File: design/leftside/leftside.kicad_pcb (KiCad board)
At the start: 4 copper layers, 142.6 x 96.2 mm, 227 parts, among them IC2 XC9148G50CER-G, IC3 nRF52833-QDAA-R7, IC4 74AHCT125PW,118, IC5 MCP23018T-E_SS, IC6 XC9291B33D1R-G, J1 USB_C_Receptacle_USB2.0_16P, J2 Battery Pos, J3 Battery Neg, J4 OLED_128x32, J6 Conn_01x04, J7 F32Q-1A7H1-11012, U1 BQ27441-G1, U2 BQ24072RGT, U3 USB6B1, U5 PEC11L-4015F-S0015, U6 PEC11L-4015F-S0015, Y1 ECS-320-8-37B2-JTY-TR

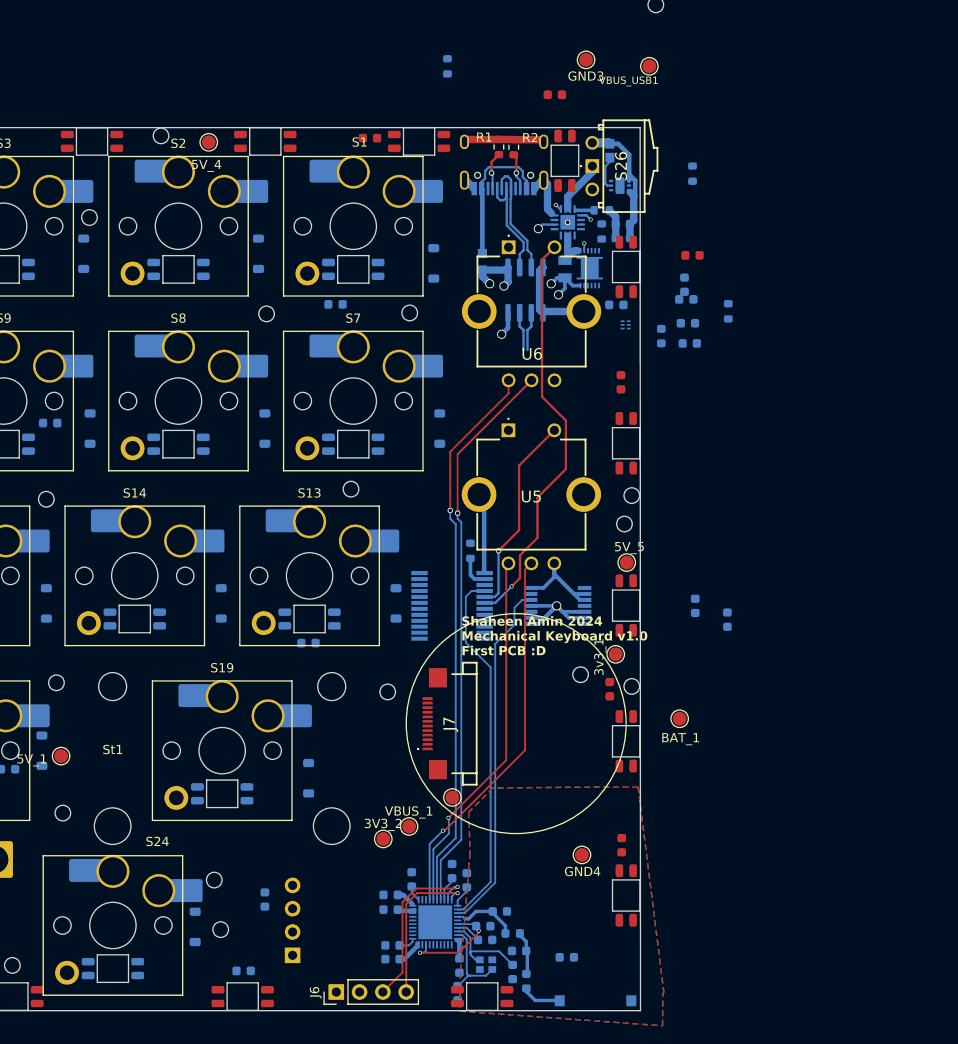
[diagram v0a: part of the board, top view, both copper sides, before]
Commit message: begin to move power plane
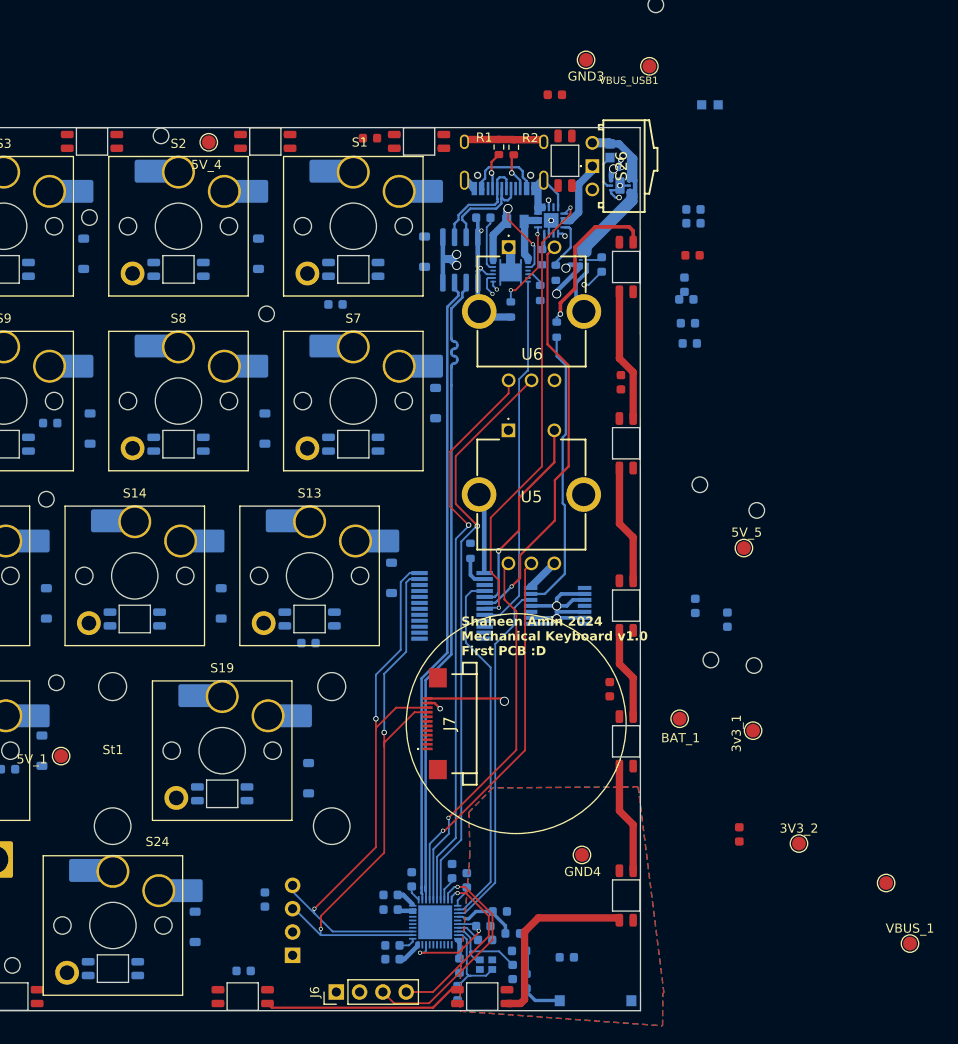
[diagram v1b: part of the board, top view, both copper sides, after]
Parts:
- removed the REF** at (198.6, 116.5)
- removed the REF** at (201.0, 75.2)
- removed the REF** at (179.7, 137.0)
- removed the REF** at (180.4, 142.4)
- removed the REF** at (194.6, 94.4)
- removed the REF** at (163.2, 129.7)
- moved VBUS_1 56.1 mm to (255.5, 143.9)
- moved GND2 48.2 mm to (252.9, 137.3)
- moved 3V3_2 45.3 mm to (243.4, 133.0)
- moved R10 31.1 mm to (217.0, 77.0)
- moved F1 30.1 mm to (233.7, 52.5), turned to 180 degrees
- moved R7 20.6 mm to (215.2, 73.0), turned to 90 degrees
- moved R4 18.8 mm to (215.4, 69.1)
- moved C22 17.3 mm to (209.0, 64.8), turned to 180 degrees
- moved 3v3_1 17.1 mm to (238.4, 120.7)
- moved REF** 14.5 mm to (238.8, 96.7)
- moved REF** 14.3 mm to (233.8, 113.0)
- moved REF** 13.5 mm to (238.5, 113.6)
- moved R5 13.0 mm to (212.0, 74.8), turned to 90 degrees
- moved C39 12.9 mm to (236.9, 132.0)
- moved 5V_5 12.9 mm to (237.4, 100.8)
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- renumbered D47 to D1, D37 to D10, D46 to D2, D45 to D3, D44 to D4, D43 to D5, D42 to D6, D41 to D7, D39 to D8, D38 to D9
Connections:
- D1 pad 2: Net-(D47-DOUT) -> Net-(D1-DOUT)
- D1 pad 4: Net-(D46-DOUT) -> Net-(D1-DIN)
- D10 pad 2: Net-(D37-DOUT) -> Net-(D10-DOUT)
- D10 pad 4: Net-(D36-DOUT) -> Net-(D10-DIN)
- D2 pad 2: Net-(D46-DOUT) -> Net-(D2-DOUT)
- D2 pad 4: Net-(D45-DOUT) -> Net-(D1-DOUT)
- D3 pad 2: Net-(D45-DOUT) -> Net-(D3-DOUT)
- D3 pad 4: Net-(D44-DOUT) -> Net-(D2-DOUT)
- D4 pad 2: Net-(D44-DOUT) -> Net-(D4-DOUT)
- D4 pad 4: Net-(D43-DOUT) -> Net-(D3-DOUT)
- D5 pad 2: Net-(D43-DOUT) -> Net-(D5-DOUT)
- D5 pad 4: Net-(D42-DOUT) -> Net-(D4-DOUT)
- D6 pad 2: Net-(D42-DOUT) -> Net-(D6-DOUT)
- D6 pad 4: Net-(D41-DOUT) -> Net-(D5-DOUT)
- D7 pad 2: Net-(D41-DOUT) -> Net-(D7-DOUT)
- D7 pad 4: Net-(D40-DOUT) -> Net-(D6-DOUT)
- D8 pad 2: Net-(D39-DOUT) -> Net-(D8-DOUT)
- D8 pad 4: Net-(D38-DOUT) -> Net-(D7-DOUT)
- D9 pad 2: Net-(D38-DOUT) -> Net-(D10-DIN)
- D9 pad 4: Net-(D37-DOUT) -> Net-(D8-DOUT)
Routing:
- net /SCL: track 0.00 -> 67.3 mm, vias 0 -> 3
- net D+: track 4.20 -> 70.9 mm
- net /SDA: track 0.00 -> 65.8 mm, vias 0 -> 3
- net D-: track 4.20 -> 69.1 mm
- net /CHG: track 0.74 -> 50.1 mm, vias 1 -> 2
- net /GPOUT: track 0.00 -> 39.3 mm
- net Net-(IC4-2Y): track 0.00 -> 31.1 mm
- net Net-(IC2-BAT): track 15.3 -> 43.0 mm
- net Net-(D6-DOUT): track 0.00 -> 21.7 mm
- net Net-(D5-DOUT): track 0.00 -> 20.6 mm
- net GND: track 70.6 -> 89.7 mm, vias 2 -> 8
- net 3V3: track 11.3 -> 30.1 mm, vias 0 -> 4
- net Net-(D1-DIN): track 0.00 -> 17.7 mm, vias 0 -> 1
- net Net-(D1-DOUT): track 0.00 -> 14.4 mm
- net Net-(D2-DOUT): track 0.00 -> 12.9 mm
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
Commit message: LS: prepare to flip 5V dcdc
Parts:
- removed the REF** at (108.0, 75.8)
- removed the REF** at (142.5, 95.8)
- removed the REF** at (161.4, 95.5)
- removed the REF** at (104.4, 113.4)
- removed the REF** at (133.4, 132.6)
- removed the REF** at (173.9, 55.9)
- removed the REF** at (162.5, 115.5)
- removed the REF** at (123.4, 95.6)
- removed the REF** at (104.3, 128.8)
- removed the REF** at (157.7, 146.3)
- removed the REF** at (104.4, 95.4)
- removed the REF** at (142.5, 128.8)
- removed the REF** at (108.0, 84.1)
- removed the REF** at (147.2, 75.6)
- removed the REF** at (185.4, 75.3)
- C20, C31, C38, C45, C9: moved to F.Cu
- C26, C36, C42: moved to B.Cu
- moved 3V3_2 190.5 mm to (52.9, 134.2)
- moved 3v3_1 190.5 mm to (47.9, 121.9)
- moved 5V_5 190.5 mm to (46.9, 102.0)
- moved BAT_1 190.5 mm to (39.9, 120.6)
- moved C13 190.5 mm to (40.8, 77.5)
- moved C18 190.5 mm to (41.0, 79.7)
- moved C24 190.5 mm to (40.4, 73.3)
- moved GND2 190.5 mm to (62.4, 138.5)
- moved REF** 190.5 mm to (43.3, 114.2)
- moved REF** 190.5 mm to (42.1, 95.1)
- moved REF** 190.5 mm to (48.0, 114.8)
- moved REF** 190.5 mm to (48.3, 97.9)
- moved VBUS_1 190.5 mm to (65.0, 145.1)
- moved C37 157.9 mm to (68.2, 83.8), turned to 90 degrees
- moved C45 124.8 mm to (84.6, 70.0), turned to 90 degrees
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- renumbered D9 to D10, D10 to D11, D36 to D12, D35 to D13, D34 to D14, D33 to D15, D32 to D16, D31 to D17, D30 to D18, D29 to D19, D28 to D20, D27 to D21, D26 to D22, D25 to D23, D23 to D25, D22 to D26, D21 to D27, D20 to D28, D19 to D29, D18 to D30, D17 to D31, D16 to D32, D15 to D33, D14 to D34, D13 to D35, D12 to D36, D11 to D37, D10 to D38, D9 to D39, D8 to D40, D7 to D41, D6 to D42, D5 to D43, D4 to D44, D3 to D45, D2 to D46, D1 to D47, D40 to D8, D8 to D9
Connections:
- D10 pad 2: Net-(D10-DIN) -> Net-(D10-DOUT)
- D10 pad 4: Net-(D8-DOUT) -> Net-(D10-DIN)
- D11 pad 2: Net-(D10-DOUT) -> Net-(D11-DOUT)
- D11 pad 4: Net-(D10-DIN) -> Net-(D10-DOUT)
- D12 pad 2: Net-(D36-DOUT) -> Net-(D12-DOUT)
- D12 pad 4: Net-(D35-DOUT) -> Net-(D11-DOUT)
- D13 pad 2: Net-(D35-DOUT) -> Net-(D13-DOUT)
- D13 pad 4: Net-(D34-DOUT) -> Net-(D12-DOUT)
- D14 pad 2: Net-(D34-DOUT) -> Net-(D14-DOUT)
- D14 pad 4: Net-(D33-DOUT) -> Net-(D13-DOUT)
- D15 pad 2: Net-(D33-DOUT) -> Net-(D15-DOUT)
- D15 pad 4: Net-(D32-DOUT) -> Net-(D14-DOUT)
- D16 pad 2: Net-(D32-DOUT) -> Net-(D16-DOUT)
- D16 pad 4: Net-(D31-DOUT) -> Net-(D15-DOUT)
- D17 pad 2: Net-(D31-DOUT) -> Net-(D17-DOUT)
- D17 pad 4: Net-(D30-DOUT) -> Net-(D16-DOUT)
- D18 pad 2: Net-(D30-DOUT) -> Net-(D18-DOUT)
- D18 pad 4: Net-(D29-DOUT) -> Net-(D17-DOUT)
- D19 pad 2: Net-(D29-DOUT) -> Net-(D19-DOUT)
- D19 pad 4: Net-(D28-DOUT) -> Net-(D18-DOUT)
- D20 pad 2: Net-(D28-DOUT) -> Net-(D20-DOUT)
- D20 pad 4: Net-(D27-DOUT) -> Net-(D19-DOUT)
- D21 pad 2: Net-(D27-DOUT) -> Net-(D21-DOUT)
- D21 pad 4: Net-(D26-DOUT) -> Net-(D20-DOUT)
- D22 pad 2: Net-(D26-DOUT) -> Net-(D22-DOUT)
- D22 pad 4: Net-(D25-DOUT) -> Net-(D21-DOUT)
- D23 pad 2: Net-(D25-DOUT) -> Net-(D23-DOUT)
- D23 pad 4: Net-(D24-DOUT) -> Net-(D22-DOUT)
- D25 pad 2: Net-(D23-DOUT) -> Net-(D25-DOUT)
- D25 pad 4: Net-(D22-DOUT) -> Net-(D24-DOUT)
- D26 pad 2: Net-(D22-DOUT) -> Net-(D26-DOUT)
- D26 pad 4: Net-(D21-DOUT) -> Net-(D25-DOUT)
- D27 pad 2: Net-(D21-DOUT) -> Net-(D27-DOUT)
- D27 pad 4: Net-(D20-DOUT) -> Net-(D26-DOUT)
- D28 pad 2: Net-(D20-DOUT) -> Net-(D28-DOUT)
- D28 pad 4: Net-(D19-DOUT) -> Net-(D27-DOUT)
- D29 pad 2: Net-(D19-DOUT) -> Net-(D29-DOUT)
- D29 pad 4: Net-(D18-DOUT) -> Net-(D28-DOUT)
- D30 pad 2: Net-(D18-DOUT) -> Net-(D30-DOUT)
- D30 pad 4: Net-(D17-DOUT) -> Net-(D29-DOUT)
- D31 pad 2: Net-(D17-DOUT) -> Net-(D31-DOUT)
- D31 pad 4: Net-(D16-DOUT) -> Net-(D30-DOUT)
- D32 pad 2: Net-(D16-DOUT) -> Net-(D32-DOUT)
- D32 pad 4: Net-(D15-DOUT) -> Net-(D31-DOUT)
- D33 pad 2: Net-(D15-DOUT) -> Net-(D33-DOUT)
- D33 pad 4: Net-(D14-DOUT) -> Net-(D32-DOUT)
- D34 pad 2: Net-(D14-DOUT) -> Net-(D34-DOUT)
- D34 pad 4: Net-(D13-DOUT) -> Net-(D33-DOUT)
- D35 pad 2: Net-(D13-DOUT) -> Net-(D35-DOUT)
- D35 pad 4: Net-(D12-DOUT) -> Net-(D34-DOUT)
- D36 pad 2: Net-(D12-DOUT) -> Net-(D36-DOUT)
- D36 pad 4: Net-(D11-DOUT) -> Net-(D35-DOUT)
- D37 pad 2: Net-(D11-DOUT) -> Net-(D37-DOUT)
- D37 pad 4: Net-(D10-DOUT) -> Net-(D36-DOUT)
- D38 pad 2: Net-(D10-DOUT) -> Net-(D38-DOUT)
- D38 pad 4: Net-(D10-DIN) -> Net-(D37-DOUT)
- D39 pad 2: Net-(D10-DIN) -> Net-(D39-DOUT)
- D39 pad 4: Net-(D8-DOUT) -> Net-(D38-DOUT)
- D40 pad 2: Net-(D8-DOUT) -> Net-(D40-DOUT)
- D40 pad 4: Net-(D7-DOUT) -> Net-(D39-DOUT)
- D41 pad 2: Net-(D7-DOUT) -> Net-(D41-DOUT)
- D41 pad 4: Net-(D6-DOUT) -> Net-(D40-DOUT)
- D42 pad 2: Net-(D6-DOUT) -> Net-(D42-DOUT)
- D42 pad 4: Net-(D5-DOUT) -> Net-(D41-DOUT)
- D43 pad 2: Net-(D5-DOUT) -> Net-(D43-DOUT)
- D43 pad 4: Net-(D4-DOUT) -> Net-(D42-DOUT)
- D44 pad 2: Net-(D4-DOUT) -> Net-(D44-DOUT)
- D44 pad 4: Net-(D3-DOUT) -> Net-(D43-DOUT)
- D45 pad 2: Net-(D3-DOUT) -> Net-(D45-DOUT)
- D45 pad 4: Net-(D2-DOUT) -> Net-(D44-DOUT)
- D46 pad 2: Net-(D2-DOUT) -> Net-(D46-DOUT)
- D46 pad 4: Net-(D1-DOUT) -> Net-(D45-DOUT)
- D47 pad 2: Net-(D1-DOUT) -> Net-(D47-DOUT)
- D47 pad 4: Net-(D1-DIN) -> Net-(D46-DOUT)
- D8 pad 2: Net-(D40-DOUT) -> Net-(D8-DOUT)
- D8 pad 4: Net-(D39-DOUT) -> Net-(D7-DOUT)
- D9 pad 2: Net-(D8-DOUT) -> Net-(D10-DIN)
- D9 pad 4: Net-(D7-DOUT) -> Net-(D8-DOUT)
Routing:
- net /Row 0: track 0.00 -> 221.6 mm, vias 0 -> 2
- net /Column 5: track 0.00 -> 204.4 mm, vias 0 -> 1
- net /Row 1: track 0.00 -> 181.6 mm, vias 0 -> 2
- net /Column 4: track 0.00 -> 181.5 mm, vias 0 -> 1
- net /Column 3: track 0.00 -> 169.4 mm, vias 0 -> 1
- net /Row 2: track 0.00 -> 152.8 mm, vias 0 -> 2
- net /Column 2: track 0.00 -> 142.3 mm, vias 0 -> 1
- net /Column 1: track 0.00 -> 127.2 mm, vias 0 -> 1
- net /Row 3: track 0.00 -> 126.4 mm
- net /Column 0: track 0.00 -> 114.1 mm, vias 0 -> 1
- net 5V: track 6.00 -> 107.9 mm, vias 3 -> 29
- net GND: track 89.7 -> 185.0 mm, vias 8 -> 64
- net /SCL: track 67.3 -> 105.3 mm, vias 3 -> 4
- net /SDA: track 65.8 -> 101.1 mm, vias 3 -> 4
- net Net-(D26-DOUT): track 0.00 -> 34.1 mm
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
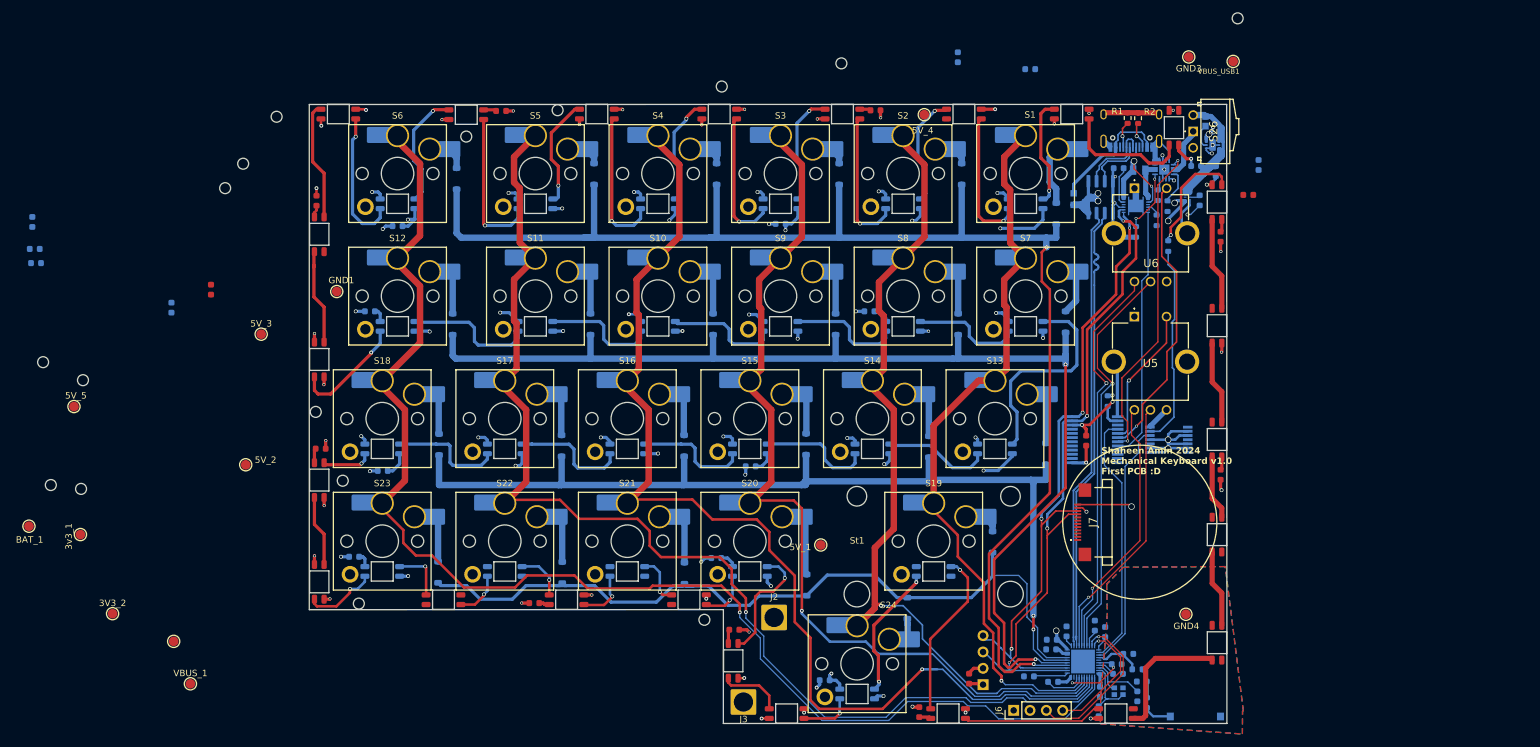
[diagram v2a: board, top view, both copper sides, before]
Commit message: LS routing complete
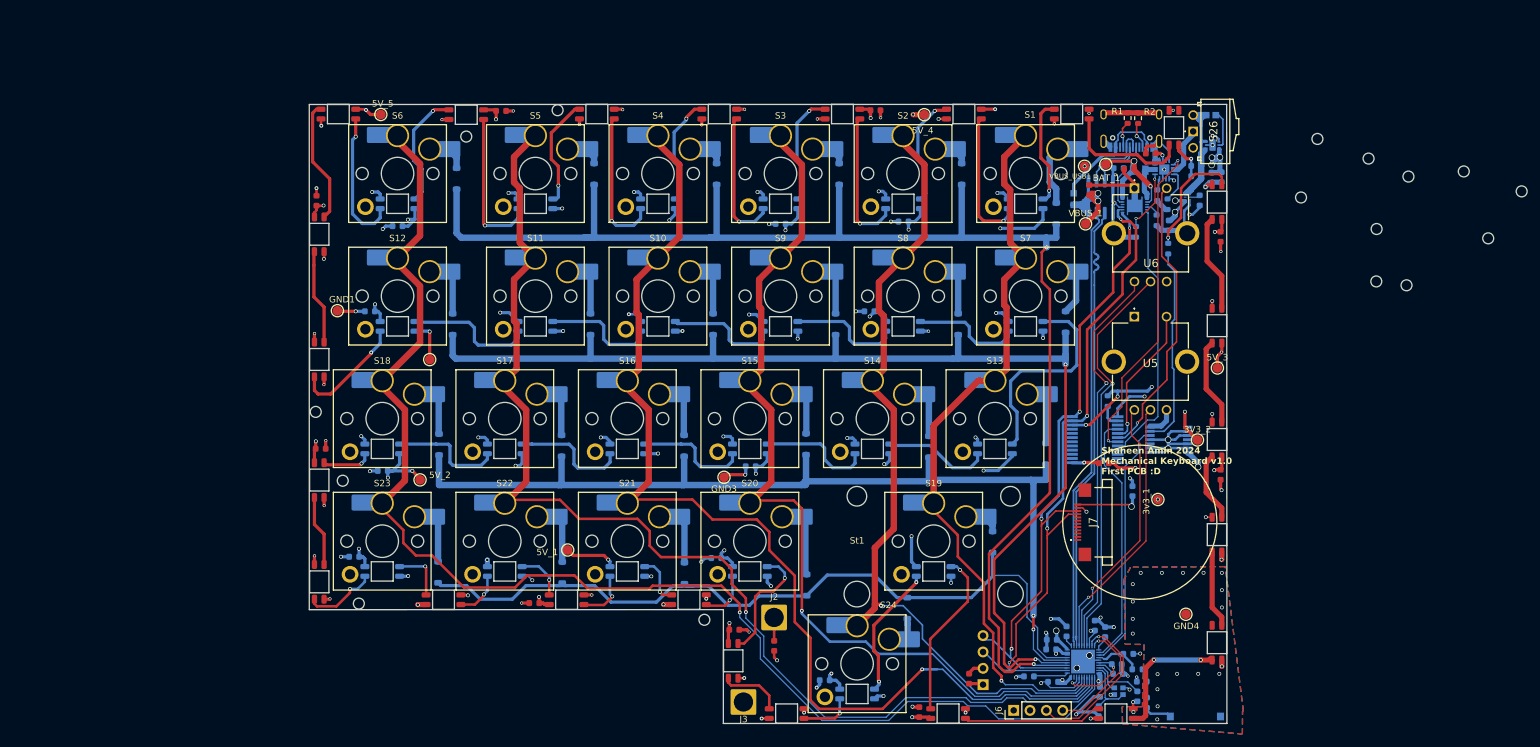
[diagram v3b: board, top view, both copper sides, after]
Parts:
- C17, C18, C23, C24: moved to F.Cu
- C27, C37: moved to B.Cu
- moved REF** 208.5 mm to (249.4, 82.5)
- moved REF** 208.5 mm to (248.2, 63.4)
- moved REF** 208.5 mm to (254.1, 83.1)
- moved REF** 208.5 mm to (254.4, 66.2)
- moved REF** 193.9 mm to (272.0, 68.5)
- moved REF** 193.9 mm to (266.8, 75.8)
- moved REF** 192.6 mm to (263.0, 65.4)
- moved BAT_1 176.6 mm to (207.3, 64.3)
- moved C13 176.3 mm to (217.1, 73.8), turned to 90 degrees
- moved 3V3_2 170.8 mm to (221.6, 107.2)
- moved C18 170.6 mm to (210.9, 65.1), turned to 180 degrees
- moved 3v3_1 167.6 mm to (215.4, 116.4)
- moved C24 164.4 mm to (204.8, 68.3), turned to 90 degrees
- moved VBUS_1 156.4 mm to (204.2, 73.6)
- moved 5V_3 148.7 mm to (224.7, 96.0)
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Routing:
- net GND: track 185.0 -> 271.5 mm, vias 64 -> 111
- net 5V: track 107.9 -> 167.5 mm, vias 29 -> 54
- net 3V3: track 43.2 -> 64.4 mm, vias 7 -> 14
- net Net-(IC2-BAT): track 45.1 -> 25.5 mm
- net /VBUS: track 22.2 -> 30.9 mm
- net /BAT: track 14.4 -> 22.6 mm
- net Net-(IC2-LX): track 3.79 -> 5.92 mm
- net /GPOUT: track 39.3 -> 40.9 mm
- net Net-(D26-DOUT): track 34.1 -> 33.1 mm
- net /VBUS_USB: track 19.6 -> 20.5 mm, vias 0 -> 1
- net Net-(D3-DOUT): track 10.0 -> 10.8 mm
- net Net-(D2-DOUT): track 12.9 -> 13.7 mm
- net Net-(D34-DOUT): track 18.4 -> 19.1 mm
- net Net-(D1-DOUT): track 14.4 -> 15.1 mm
- net /DEC4_6: track 11.6 -> 12.3 mm
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
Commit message: LS RS no error
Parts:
- added REF**: M1.6 Hole, CustomLibrary:M1.6 Hole, F.Cu at (182.6, 138.6)
- added REF**: M1.6 Hole, CustomLibrary:M1.6 Hole, F.Cu at (104.4, 94.4)
- added REF**: M1.6 Hole, CustomLibrary:M1.6 Hole, F.Cu at (201.7, 75.4)
- added REF**: M1.6 Hole, CustomLibrary:M1.6 Hole, F.Cu at (198.5, 132.1)
- added REF**: M1.6 Hole, CustomLibrary:M1.6 Hole, F.Cu at (86.4, 62.5)
- moved REF** 156.6 mm to (99.8, 55.9)
- moved REF** 155.4 mm to (107.9, 75.3)
- moved REF** 116.9 mm to (188.5, 150.4)
- moved REF** 115.4 mm to (142.5, 94.4)
- moved REF** 113.3 mm to (148.8, 134.7)
- moved REF** 82.7 mm to (166.3, 75.1)
- moved REF** 57.6 mm to (225.3, 115.8)
- moved REF** 57.5 mm to (195.0, 55.9)
- moved REF** 56.8 mm to (219.3, 113.2)
- moved REF** 16.7 mm to (225.2, 80.6)
- moved REF** 16.2 mm to (138.3, 55.9)
- moved REF** 10.7 mm to (134.5, 132.6)
- moved GND2 6.55 mm to (95.7, 94.2)
- moved Di21 3.16 mm to (160.5, 126.6)
- moved J2 2.06 mm to (157.8, 134.6)
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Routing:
- net Net-(Di21-A): track 9.38 -> 6.18 mm
- net /Row 0: track 221.6 -> 218.9 mm
- net /Row 3: track 126.4 -> 127.7 mm
- net /Column 2: track 142.3 -> 143.5 mm
- net GND: track 271.5 -> 270.3 mm
- net Net-(D6-DOUT): track 21.6 -> 22.8 mm
- net Net-(D43-DOUT): track 22.2 -> 21.1 mm
- net /BAT: track 22.6 -> 23.6 mm
- net Net-(D1-DIN): track 18.1 -> 17.2 mm
- net 5V: track 167.5 -> 168.2 mm
- net Net-(D11-DOUT): track 18.8 -> 19.4 mm
- added copper zone on B.Cu, net Net-(IC3-ANT)
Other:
- board text added: "Shaheen. A 2024 Mechanical Keyboard v1.0 First PCB :D"
- board text removed: "Shaheen Amin 2024 Mechanical Keyboard v1.0 First PCB :D"
